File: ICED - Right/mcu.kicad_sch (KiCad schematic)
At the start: 48 parts, among them P1 FLASH_HDR, P2 USBC, P3 CONN_17, P4 USB3_AFEMALE, P5 RGB Out, Q1 TC1264, U1 MK20DX256VLH7, X1 CRYSTAL

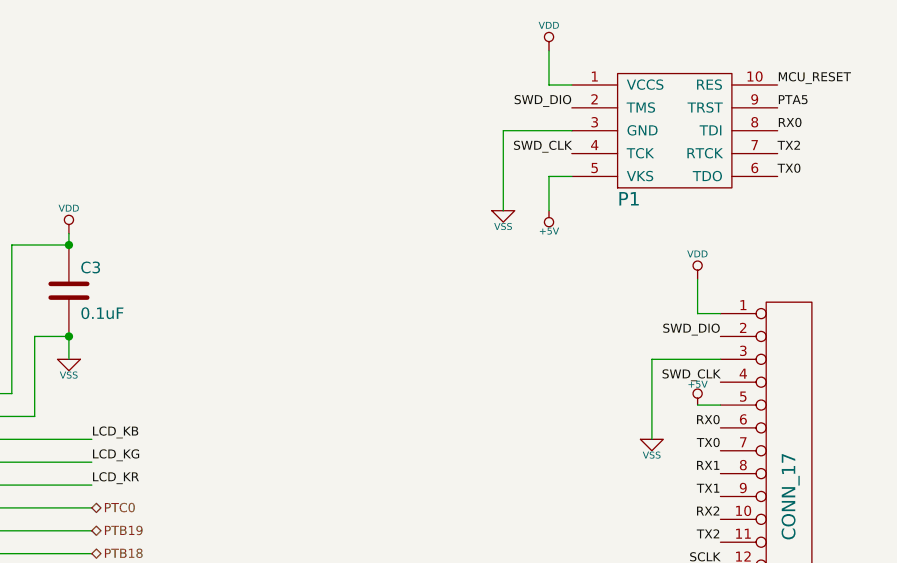
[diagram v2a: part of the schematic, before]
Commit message: Change J-Link connector
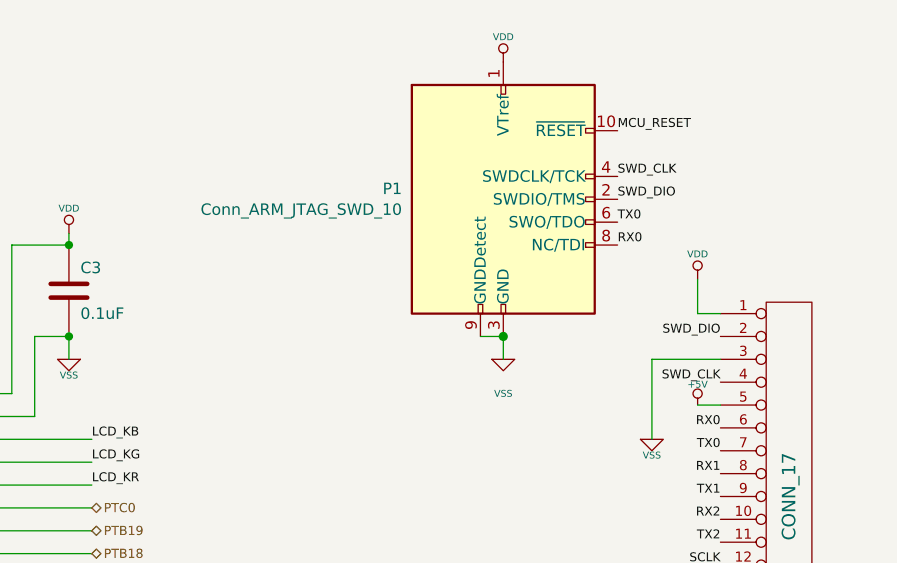
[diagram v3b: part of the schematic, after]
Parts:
- removed P1: FLASH_HDR, prettylib:JLINK_NEEDLE, symbol ICEDRight:FLASH_HDR
- added P1: Conn_ARM_JTAG_SWD_10, prettylib:SHF-105-01-L-D-TH, symbol Connector:Conn_ARM_JTAG_SWD_10
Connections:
- net MCU_RESET: now also P1.10 (~{RESET})
- net RX0: now also P1.8 (NC/TDI)
- net SWD_CLK: now also P1.4 (SWDCLK/TCK)
- net SWD_DIO: now also P1.2 (SWDIO/TMS)
- net TX0: now also P1.6 (SWO/TDO)
- net VDD: now also P1.1 (VTref)
- net VSS: now also P1.3 (GND), P1.5 (GND), P1.9 (GNDDetect)
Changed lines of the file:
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@@
   (junction (at 242.57 114.3) (diameter 1.016) (color 0 0 0 0))
   (junction (at 242.57 127) (diameter 1.016) (color 0 0 0 0))
+  (junction (at 245.11 48.26) (diameter 1.016) (color 0 0 0 0))
   (junction (at 245.11 137.16) (diameter 1.016) (color 0 0 0 0))
   (junction (at 245.11 156.21) (diameter 1.016) (color 0 0 0 0))
@@
     (stroke (width 0) (type default) (color 0 0 0 0))
   )
+  (wire (pts (xy 242.57 48.26) (xy 245.11 48.26))
+    (stroke (width 0) (type solid) (color 0 0 0 0))
+  )
   (wire (pts (xy 242.57 101.6) (xy 237.49 101.6))
     (stroke (width 0) (type solid) (color 0 0 0 0))
@@
     (stroke (width 0) (type solid) (color 0 0 0 0))
   )
-  (wire (pts (xy 245.11 25.4) (xy 245.11 34.29))
-    (stroke (width 0) (type default) (color 0 0 0 0))
+  (wire (pts (xy 245.11 50.8) (xy 245.11 48.26))
+    (stroke (width 0) (type solid) (color 0 0 0 0))
   )
   (wire (pts (xy 245.11 149.86) (xy 245.11 156.21))
@@
     (stroke (width 0) (type solid) (color 0 0 0 0))
   )
-  (wire (pts (xy 250.19 20.32) (xy 250.19 16.51))
-    (stroke (width 0) (type default) (color 0 0 0 0))
-  )
-  (wire (pts (xy 250.19 30.48) (xy 250.19 34.29))
-    (stroke (width 0) (type default) (color 0 0 0 0))
-  )
   (wire (pts (xy 250.19 137.16) (xy 245.11 137.16))
     (stroke (width 0) (type solid) (color 0 0 0 0))
@@
   (wire (pts (xy 250.19 173.99) (xy 250.19 171.45))
     (stroke (width 0) (type solid) (color 0 0 0 0))
-  )
-  (wire (pts (xy 252.73 20.32) (xy 250.19 20.32))
-    (stroke (width 0) (type default) (color 0 0 0 0))
-  )
-  (wire (pts (xy 252.73 25.4) (xy 245.11 25.4))
-    (stroke (width 0) (type default) (color 0 0 0 0))
-  )
-  (wire (pts (xy 252.73 30.48) (xy 250.19 30.48))
-    (stroke (width 0) (type default) (color 0 0 0 0))
   )
   (wire (pts (xy 255.27 149.86) (xy 255.27 151.13))
@@
     (effects (font (size 0.9906 0.9906)) (justify right bottom))
   )
-  (label "SWD_DIO" (at 252.73 22.86 180)
-    (effects (font (size 0.9906 0.9906)) (justify right bottom))
-  )
-  (label "SWD_CLK" (at 252.73 27.94 180)
-    (effects (font (size 0.9906 0.9906)) (justify right bottom))
+  (label "MCU_RESET" (at 257.81 25.4 0)
+    (effects (font (size 0.9906 0.9906)) (justify left bottom))
+  )
+  (label "SWD_CLK" (at 257.81 30.48 0)
+    (effects (font (size 0.9906 0.9906)) (justify left bottom))
+  )
+  (label "SWD_DIO" (at 257.81 33.02 0)
+    (effects (font (size 0.9906 0.9906)) (justify left bottom))
+  )
+  (label "TX0" (at 257.81 35.56 0)
+    (effects (font (size 0.9906 0.9906)) (justify left bottom))
+  )
+  (label "RX0" (at 257.81 38.1 0)
+    (effects (font (size 0.9906 0.9906)) (justify left bottom))
   )
   (label "SWD_DIO" (at 269.24 48.26 180)
@@
   (label "RGBOUT" (at 269.24 86.36 180)
     (effects (font (size 0.9906 0.9906)) (justify right bottom))
-  )
-  (label "MCU_RESET" (at 275.59 20.32 0)
-    (effects (font (size 0.9906 0.9906)) (justify left bottom))
-  )
-  (label "PTA5" (at 275.59 22.86 0)
-    (effects (font (size 0.9906 0.9906)) (justify left bottom))
-  )
-  (label "RX0" (at 275.59 25.4 0)
-    (effects (font (size 0.9906 0.9906)) (justify left bottom))
-  )
-  (label "TX2" (at 275.59 27.94 0)
-    (effects (font (size 0.9906 0.9906)) (justify left bottom))
-  )
-  (label "TX0" (at 275.59 30.48 0)
-    (effects (font (size 0.9906 0.9906)) (justify left bottom))
   )
   (hierarchical_label "GND" (shape bidirectional) (at 26.67 53.34 270)
@@
     (pin "1")
   )
-  (symbol (lib_id "ICEDRight:+5V") (at 250.19 34.29 180) (unit 1)
-    (in_bom yes) (on_board yes)
-    (property "Reference" "#PWR011" (id 0) (at 250.19 36.576 0)
-      (effects (font (size 0.508 0.508)) hide)
-    )
-    (property "Value" "+5V" (id 1) (at 250.19 36.576 0)
-      (effects (font (size 0.762 0.762)))
-    )
-    (property "Footprint" "" (id 2) (at 250.19 34.29 0)
-      (effects (font (size 1.524 1.524)))
-    )
-    (property "Datasheet" "" (id 3) (at 250.19 34.29 0)
-      (effects (font (size 1.524 1.524)))
-    )
-    (pin "1")
-  )
   (symbol (lib_id "ICEDRight:+5V") (at 266.7 55.88 0) (unit 1)
     (in_bom yes) (on_board yes)
@@
     (pin "1")
   )
+  (symbol (lib_id "ICEDLeft:VDD") (at 245.11 17.78 0) (unit 1)
+    (in_bom yes) (on_board yes)
+    (property "Reference" "#PWR0111" (id 0) (at 245.11 15.24 0)
+      (effects (font (size 0.762 0.762)) hide)
+    )
+    (property "Value" "VDD" (id 1) (at 245.11 14.986 0)
+      (effects (font (size 0.762 0.762)))
+    )
+    (property "Footprint" "" (id 2) (at 245.11 17.78 0)
+      (effects (font (size 1.524 1.524)))
+    )
+    (property "Datasheet" "" (id 3) (at 245.11 17.78 0)
+      (effects (font (size 1.524 1.524)))
+    )
+    (pin "1")
+  )
   (symbol (lib_id "ICEDLeft:VDD") (at 245.11 137.16 0) (unit 1)
     (in_bom yes) (on_board yes)
@@
     (pin "1")
   )
-  (symbol (lib_id "ICEDRight:VDD") (at 250.19 16.51 0) (unit 1)
-    (in_bom yes) (on_board yes)
-    (property "Reference" "#PWR028" (id 0) (at 250.19 13.97 0)
-      (effects (font (size 0.762 0.762)) hide)
-    )
-    (property "Value" "VDD" (id 1) (at 250.19 13.716 0)
-      (effects (font (size 0.762 0.762)))
-    )
-    (property "Footprint" "" (id 2) (at 250.19 16.51 0)
-      (effects (font (size 1.524 1.524)))
-    )
-    (property "Datasheet" "" (id 3) (at 250.19 16.51 0)
-      (effects (font (size 1.524 1.524)))
-    )
-    (pin "1")
-  )
   (symbol (lib_id "ICEDRight:VDD") (at 266.7 41.91 0) (unit 1)
     (in_bom yes) (on_board yes)
@@
     (pin "1")
   )
-  (symbol (lib_id "ICEDRight:VSS") (at 245.11 34.29 0) (unit 1)
-    (in_bom yes) (on_board yes)
-    (property "Reference" "#PWR09" (id 0) (at 245.11 34.29 0)
-      (effects (font (size 0.762 0.762)) hide)
-    )
-    (property "Value" "VSS" (id 1) (at 245.11 36.068 0)
-      (effects (font (size 0.762 0.762)))
-    )
-    (property "Footprint" "" (id 2) (at 245.11 34.29 0)
-      (effects (font (size 1.524 1.524)))
-    )
-    (property "Datasheet" "" (id 3) (at 245.11 34.29 0)
+  (symbol (lib_id "ICEDLeft:VSS") (at 245.11 50.8 0) (unit 1)
+    (in_bom yes) (on_board yes)
+    (property "Reference" "#PWR0112" (id 0) (at 245.11 50.8 0)
+      (effects (font (size 0.762 0.762)) hide)
+    )
+    (property "Value" "VSS" (id 1) (at 245.11 54.61 0)
+      (effects (font (size 0.762 0.762)))
+    )
+    (property "Footprint" "" (id 2) (at 245.11 50.8 0)
+      (effects (font (size 1.524 1.524)))
+    )
+    (property "Datasheet" "" (id 3) (at 245.11 50.8 0)
       (effects (font (size 1.524 1.524)))
     )
@@
     (pin "2")
     (pin "3")
-  )
-  (symbol (lib_id "ICEDRight:FLASH_HDR") (at 264.16 25.4 0) (unit 1)
-    (in_bom yes) (on_board yes)
-    (property "Reference" "P1" (id 0) (at 259.08 33.02 0)
-      (effects (font (size 1.4986 1.4986)))
-    )
-    (property "Value" "FLASH_HDR" (id 1) (at 264.16 25.4 90)
-      (effects (font (size 1.4986 1.4986)) hide)
-    )
-    (property "Footprint" "prettylib:JLINK_NEEDLE" (id 2) (at 264.16 25.4 0)
-      (effects (font (size 1.524 1.524)) hide)
-    )
-    (property "Datasheet" "" (id 3) (at 264.16 25.4 0)
-      (effects (font (size 1.524 1.524)))
-    )
-    (property "Field4" "Dual-row" (id 4) (at 258.318 31.242 0)
-      (effects (font (size 0.127 0.127)) (justify left bottom) hide)
-    )
-    (pin "1")
-    (pin "10")
-    (pin "2")
-    (pin "3")
-    (pin "4")
-    (pin "5")
-    (pin "6")
-    (pin "7")
-    (pin "8")
-    (pin "9")
   )
   (symbol (lib_id "ICEDRight:USB3") (at 27.94 90.17 0) (mirror y) (unit 1)
@@
     (pin "2")
     (pin "3")
+    (pin "4")
+    (pin "5")
+    (pin "6")
+    (pin "7")
+    (pin "8")
+    (pin "9")
+  )
+  (symbol (lib_id "Connector:Conn_ARM_JTAG_SWD_10") (at 245.11 33.02 0) (unit 1)
+    (in_bom yes) (on_board yes)
+    (property "Reference" "P1" (id 0) (at 233.8578 31.8516 0)
+      (effects (font (size 1.27 1.27)) (justify right))
+    )
+    (property "Value" "Conn_ARM_JTAG_SWD_10" (id 1) (at 233.8578 34.163 0)
+      (effects (font (size 1.27 1.27)) (justify right))
+    )
+    (property "Footprint" "prettylib:SHF-105-01-L-D-TH" (id 2) (at 245.11 33.02 0)
+      (effects (font (size 1.27 1.27)) hide)
+    )
+    (property "Datasheet" "http://infocenter.arm.com/help/topic/com.arm.doc.ddi0314h/DDI0314H_coresight_components_trm.pdf" (id 3) (at 236.22 64.77 90)
+      (effects (font (size 1.27 1.27)) hide)
+    )
+    (pin "1")
+    (pin "10")
+    (pin "2")
+    (pin "3")
